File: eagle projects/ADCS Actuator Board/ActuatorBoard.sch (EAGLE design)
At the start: 228 parts, among them J11 TE_1-84953-1, J2 TE_1-84953-1, J4 TE_1-84953-1, J5 TE-1734829-3, U1 SIP2100DY-T1-GE3, U10 LM2917MX/NOPB, U12 TSV991AILT, U13 LM2917MX/NOPB, U14 ADS7841E_2K5, U16 DRV10970_MOTOR_DRIVERDRV10970, U17 LM2917MX/NOPB, U19 TSV991AILT, U2 SIP2100DY-T1-GE3, U20 ADS7841E_2K5, U3 SIP2100DY-T1-GE3, U6 DRV10970_MOTOR_DRIVERDRV10970, U7 DRV10970_MOTOR_DRIVERDRV10970, U8 TSV991AILT, U9 ADS7841E_2K5

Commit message: Silkscreen updates
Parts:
- R11, R22, R24, R30, R42, R47, R82, R88, R89: device rcl:R-US_M0805 -> rcl:R-US_R0805
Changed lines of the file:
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@@
 <part name="TP10" library="my_library" library_urn="urn:adsk.eagle:library:22876504" deviceset="TESTPOINT" device="" package3d_urn="urn:adsk.eagle:package:24605432/3"/>
 <part name="U8" library="my_library" library_urn="urn:adsk.eagle:library:22876504" deviceset="TSV991AILT" device="" package3d_urn="urn:adsk.eagle:package:24426275/2"/>
-<part name="R11" library="rcl" library_urn="urn:adsk.eagle:library:334" deviceset="R-US_" device="M0805" package3d_urn="urn:adsk.eagle:package:23556/2" value="100R"/>
+<part name="R11" library="rcl" library_urn="urn:adsk.eagle:library:334" deviceset="R-US_" device="R0805" package3d_urn="urn:adsk.eagle:package:23553/2" value="100R"/>
 <part name="R12" library="rcl" library_urn="urn:adsk.eagle:library:334" deviceset="R-US_" device="R0402" package3d_urn="urn:adsk.eagle:package:23547/3" value="5.1k"/>
 <part name="R15" library="rcl" library_urn="urn:adsk.eagle:library:334" deviceset="R-US_" device="R0402" package3d_urn="urn:adsk.eagle:package:23547/3" value="1.8k"/>
@@
 <part name="P+11" library="supply1" library_urn="urn:adsk.eagle:library:371" deviceset="+5V" device=""/>
 <part name="JP2" library="pinhead" library_urn="urn:adsk.eagle:library:325" deviceset="PINHD-1X2" device="" package3d_urn="urn:adsk.eagle:package:22435/2"/>
-<part name="R22" library="rcl" library_urn="urn:adsk.eagle:library:334" deviceset="R-US_" device="M0805" package3d_urn="urn:adsk.eagle:package:23556/2" value="DNP"/>
-<part name="R24" library="rcl" library_urn="urn:adsk.eagle:library:334" deviceset="R-US_" device="M0805" package3d_urn="urn:adsk.eagle:package:23556/2" value="0R"/>
+<part name="R22" library="rcl" library_urn="urn:adsk.eagle:library:334" deviceset="R-US_" device="R0805" package3d_urn="urn:adsk.eagle:package:23553/2" value="DNP"/>
+<part name="R24" library="rcl" library_urn="urn:adsk.eagle:library:334" deviceset="R-US_" device="R0805" package3d_urn="urn:adsk.eagle:package:23553/2" value="0R"/>
 <part name="TP17" library="my_library" library_urn="urn:adsk.eagle:library:22876504" deviceset="TESTPOINT" device="" package3d_urn="urn:adsk.eagle:package:24605432/3"/>
 <part name="TP21" library="my_library" library_urn="urn:adsk.eagle:library:22876504" deviceset="TESTPOINT" device="" package3d_urn="urn:adsk.eagle:package:24605432/3"/>
@@
 <part name="TP30" library="my_library" library_urn="urn:adsk.eagle:library:22876504" deviceset="TESTPOINT" device="" package3d_urn="urn:adsk.eagle:package:24605432/3"/>
 <part name="U12" library="my_library" library_urn="urn:adsk.eagle:library:22876504" deviceset="TSV991AILT" device="" package3d_urn="urn:adsk.eagle:package:24426275/2"/>
-<part name="R30" library="rcl" library_urn="urn:adsk.eagle:library:334" deviceset="R-US_" device="M0805" package3d_urn="urn:adsk.eagle:package:23556/2" value="100R"/>
+<part name="R30" library="rcl" library_urn="urn:adsk.eagle:library:334" deviceset="R-US_" device="R0805" package3d_urn="urn:adsk.eagle:package:23553/2" value="100R"/>
 <part name="R31" library="rcl" library_urn="urn:adsk.eagle:library:334" deviceset="R-US_" device="R0402" package3d_urn="urn:adsk.eagle:package:23547/3" value="5.1k"/>
 <part name="R32" library="rcl" library_urn="urn:adsk.eagle:library:334" deviceset="R-US_" device="R0402" package3d_urn="urn:adsk.eagle:package:23547/3" value="1.8k"/>
@@
 <part name="P+15" library="supply1" library_urn="urn:adsk.eagle:library:371" deviceset="+5V" device=""/>
 <part name="JP3" library="pinhead" library_urn="urn:adsk.eagle:library:325" deviceset="PINHD-1X2" device="" package3d_urn="urn:adsk.eagle:package:22435/2"/>
-<part name="R42" library="rcl" library_urn="urn:adsk.eagle:library:334" deviceset="R-US_" device="M0805" package3d_urn="urn:adsk.eagle:package:23556/2" value="DNP"/>
-<part name="R47" library="rcl" library_urn="urn:adsk.eagle:library:334" deviceset="R-US_" device="M0805" package3d_urn="urn:adsk.eagle:package:23556/2" value="0R"/>
+<part name="R42" library="rcl" library_urn="urn:adsk.eagle:library:334" deviceset="R-US_" device="R0805" package3d_urn="urn:adsk.eagle:package:23553/2" value="DNP"/>
+<part name="R47" library="rcl" library_urn="urn:adsk.eagle:library:334" deviceset="R-US_" device="R0805" package3d_urn="urn:adsk.eagle:package:23553/2" value="0R"/>
 <part name="TP34" library="my_library" library_urn="urn:adsk.eagle:library:22876504" deviceset="TESTPOINT" device="" package3d_urn="urn:adsk.eagle:package:24605432/3"/>
 <part name="TP39" library="my_library" library_urn="urn:adsk.eagle:library:22876504" deviceset="TESTPOINT" device="" package3d_urn="urn:adsk.eagle:package:24605432/3"/>
@@
 <part name="TP51" library="my_library" library_urn="urn:adsk.eagle:library:22876504" deviceset="TESTPOINT" device="" package3d_urn="urn:adsk.eagle:package:24605432/3"/>
 <part name="U19" library="my_library" library_urn="urn:adsk.eagle:library:22876504" deviceset="TSV991AILT" device="" package3d_urn="urn:adsk.eagle:package:24426275/2"/>
-<part name="R82" library="rcl" library_urn="urn:adsk.eagle:library:334" deviceset="R-US_" device="M0805" package3d_urn="urn:adsk.eagle:package:23556/2" value="100R"/>
+<part name="R82" library="rcl" library_urn="urn:adsk.eagle:library:334" deviceset="R-US_" device="R0805" package3d_urn="urn:adsk.eagle:package:23553/2" value="100R"/>
 <part name="R83" library="rcl" library_urn="urn:adsk.eagle:library:334" deviceset="R-US_" device="R0402" package3d_urn="urn:adsk.eagle:package:23547/3" value="5.1k"/>
 <part name="R84" library="rcl" library_urn="urn:adsk.eagle:library:334" deviceset="R-US_" device="R0402" package3d_urn="urn:adsk.eagle:package:23547/3" value="1.8k"/>
@@
 <part name="P+24" library="supply1" library_urn="urn:adsk.eagle:library:371" deviceset="+5V" device=""/>
 <part name="JP5" library="pinhead" library_urn="urn:adsk.eagle:library:325" deviceset="PINHD-1X2" device="" package3d_urn="urn:adsk.eagle:package:22435/2"/>
-<part name="R88" library="rcl" library_urn="urn:adsk.eagle:library:334" deviceset="R-US_" device="M0805" package3d_urn="urn:adsk.eagle:package:23556/2" value="DNP"/>
-<part name="R89" library="rcl" library_urn="urn:adsk.eagle:library:334" deviceset="R-US_" device="M0805" package3d_urn="urn:adsk.eagle:package:23556/2" value="0R"/>
+<part name="R88" library="rcl" library_urn="urn:adsk.eagle:library:334" deviceset="R-US_" device="R0805" package3d_urn="urn:adsk.eagle:package:23553/2" value="DNP"/>
+<part name="R89" library="rcl" library_urn="urn:adsk.eagle:library:334" deviceset="R-US_" device="R0805" package3d_urn="urn:adsk.eagle:package:23553/2" value="0R"/>
 <part name="TP52" library="my_library" library_urn="urn:adsk.eagle:library:22876504" deviceset="TESTPOINT" device="" package3d_urn="urn:adsk.eagle:package:24605432/3"/>
 <part name="TP62" library="my_library" library_urn="urn:adsk.eagle:library:22876504" deviceset="TESTPOINT" device="" package3d_urn="urn:adsk.eagle:package:24605432/3"/>

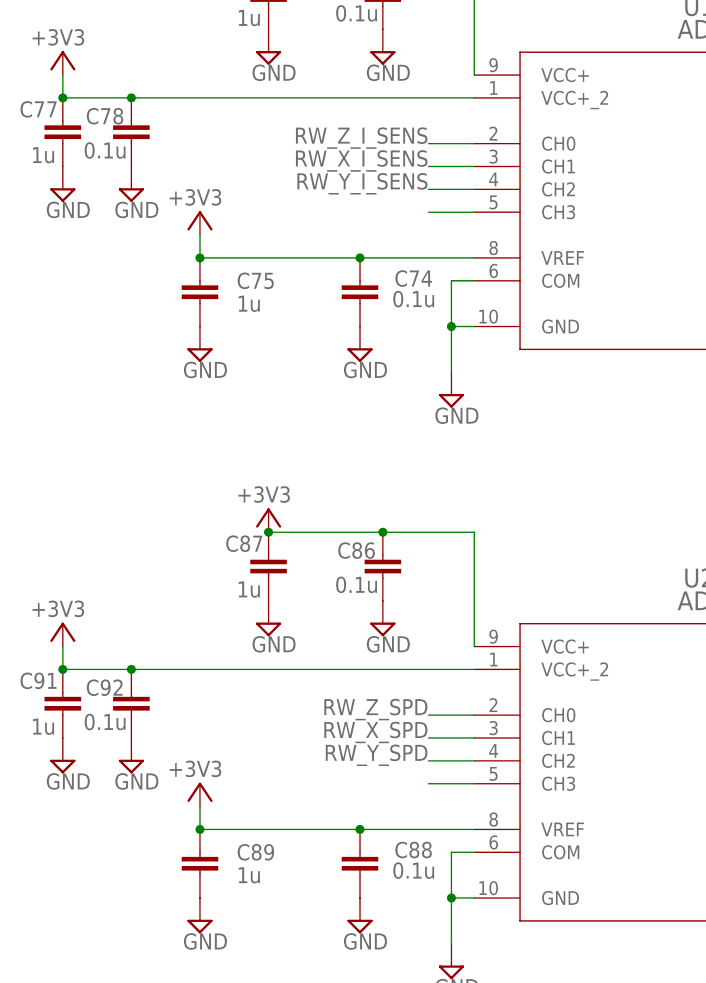
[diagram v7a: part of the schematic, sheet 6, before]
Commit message: stitching vias and silkscreen and fixed reversed totem pole driver (oops)
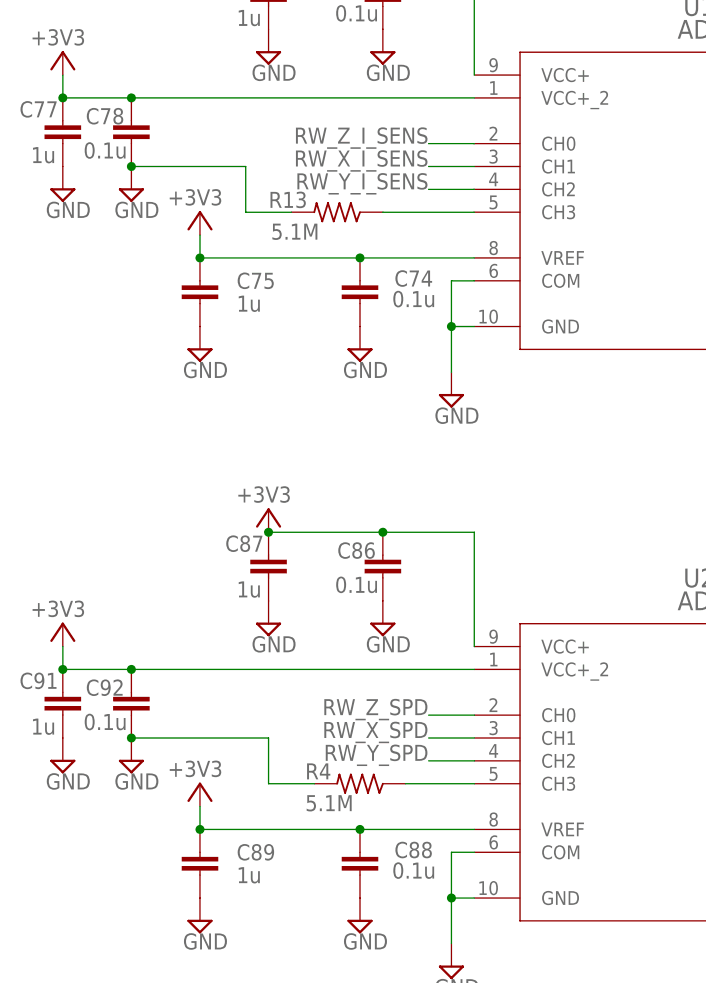
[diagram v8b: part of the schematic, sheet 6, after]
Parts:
- added R13, R14, R4: 5.1M, rcl:R-US_R0402
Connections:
- net GND: now also R13.2, R14.2, R4.2
- net N$26: now also R14.1
- net N$46: now also R13.1
- net N$60: now also R4.1
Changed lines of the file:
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@@
 <part name="P+12" library="supply1" library_urn="urn:adsk.eagle:library:371" deviceset="+5V" device=""/>
 <part name="SUPPLY19" library="supply2" library_urn="urn:adsk.eagle:library:372" deviceset="GND" device=""/>
+<part name="R4" library="rcl" library_urn="urn:adsk.eagle:library:334" deviceset="R-US_" device="R0402" package3d_urn="urn:adsk.eagle:package:23547/3" value="5.1M"/>
+<part name="R13" library="rcl" library_urn="urn:adsk.eagle:library:334" deviceset="R-US_" device="R0402" package3d_urn="urn:adsk.eagle:package:23547/3" value="5.1M"/>
+<part name="R14" library="rcl" library_urn="urn:adsk.eagle:library:334" deviceset="R-US_" device="R0402" package3d_urn="urn:adsk.eagle:package:23547/3" value="5.1M"/>
 </parts>
 <sheets>
@@
 <attribute name="VALUE" x="61.595" y="177.165" size="1.778" layer="96"/>
 </instance>
+<instance part="R14" gate="G$1" x="60.96" y="48.26" smashed="yes" rot="R180">
+<attribute name="NAME" x="53.34" y="48.4886" size="1.778" layer="95"/>
+<attribute name="VALUE" x="53.34" y="45.974" size="1.778" layer="96"/>
+</instance>
 </instances>
 <busses>
@@
 <pinref part="C71" gate="G$1" pin="2"/>
 <pinref part="SUPPLY102" gate="GND" pin="GND"/>
+<pinref part="R14" gate="G$1" pin="2"/>
+<wire x1="55.88" y1="48.26" x2="48.26" y2="48.26" width="0.1524" layer="91"/>
+<wire x1="48.26" y1="48.26" x2="48.26" y2="53.34" width="0.1524" layer="91"/>
+<wire x1="48.26" y1="53.34" x2="35.56" y2="53.34" width="0.1524" layer="91"/>
+<junction x="35.56" y="53.34"/>
 </segment>
 <segment>
@@
 <segment>
 <pinref part="U9" gate="A" pin="CH3"/>
-<wire x1="73.66" y1="48.26" x2="68.58" y2="48.26" width="0.1524" layer="91"/>
+<wire x1="73.66" y1="48.26" x2="66.04" y2="48.26" width="0.1524" layer="91"/>
+<pinref part="R14" gate="G$1" pin="1"/>
 </segment>
 </net>
@@
 <attribute name="VALUE" x="88.9" y="193.04" size="1.778" layer="96" rot="R180"/>
 </instance>
+<instance part="R4" gate="G$1" x="96.52" y="96.52" smashed="yes" rot="R180">
+<attribute name="NAME" x="90.424" y="97.0026" size="1.778" layer="95"/>
+<attribute name="VALUE" x="90.424" y="93.472" size="1.778" layer="96"/>
+</instance>
+<instance part="R13" gate="G$1" x="93.98" y="160.02" smashed="yes" rot="R180">
+<attribute name="NAME" x="86.36" y="160.5026" size="1.778" layer="95"/>
+<attribute name="VALUE" x="86.614" y="156.972" size="1.778" layer="96"/>
+</instance>
 </instances>
 <busses>
@@
 <pinref part="C78" gate="G$1" pin="2"/>
 <pinref part="SUPPLY138" gate="GND" pin="GND"/>
+<wire x1="71.12" y1="165.1" x2="83.82" y2="165.1" width="0.1524" layer="91"/>
+<junction x="71.12" y="165.1"/>
+<pinref part="R13" gate="G$1" pin="2"/>
+<wire x1="88.9" y1="160.02" x2="83.82" y2="160.02" width="0.1524" layer="91"/>
+<wire x1="83.82" y1="165.1" x2="83.82" y2="160.02" width="0.1524" layer="91"/>
 </segment>
 <segment>
@@
 <pinref part="C92" gate="G$1" pin="2"/>
 <pinref part="SUPPLY158" gate="GND" pin="GND"/>
+<wire x1="71.12" y1="101.6" x2="86.36" y2="101.6" width="0.1524" layer="91"/>
+<junction x="71.12" y="101.6"/>
+<pinref part="R4" gate="G$1" pin="2"/>
+<wire x1="91.44" y1="96.52" x2="86.36" y2="96.52" width="0.1524" layer="91"/>
+<wire x1="86.36" y1="101.6" x2="86.36" y2="96.52" width="0.1524" layer="91"/>
 </segment>
 <segment>
@@
 <segment>
 <pinref part="U14" gate="A" pin="CH3"/>
-<wire x1="109.22" y1="160.02" x2="104.14" y2="160.02" width="0.1524" layer="91"/>
+<pinref part="R13" gate="G$1" pin="1"/>
+<wire x1="99.06" y1="160.02" x2="109.22" y2="160.02" width="0.1524" layer="91"/>
 </segment>
 </net>
@@
 <segment>
 <pinref part="U20" gate="A" pin="CH3"/>
-<wire x1="109.22" y1="96.52" x2="104.14" y2="96.52" width="0.1524" layer="91"/>
+<wire x1="109.22" y1="96.52" x2="101.6" y2="96.52" width="0.1524" layer="91"/>
+<pinref part="R4" gate="G$1" pin="1"/>
 </segment>
 </net>
